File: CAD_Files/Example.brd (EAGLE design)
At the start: 86 x 54 mm, 14 parts, among them IC1 LM555D, J2 UX60-MB-5S8, Q1 BSS806N, Q2 SSM3J356R, SW1 MFS101D-6-Z

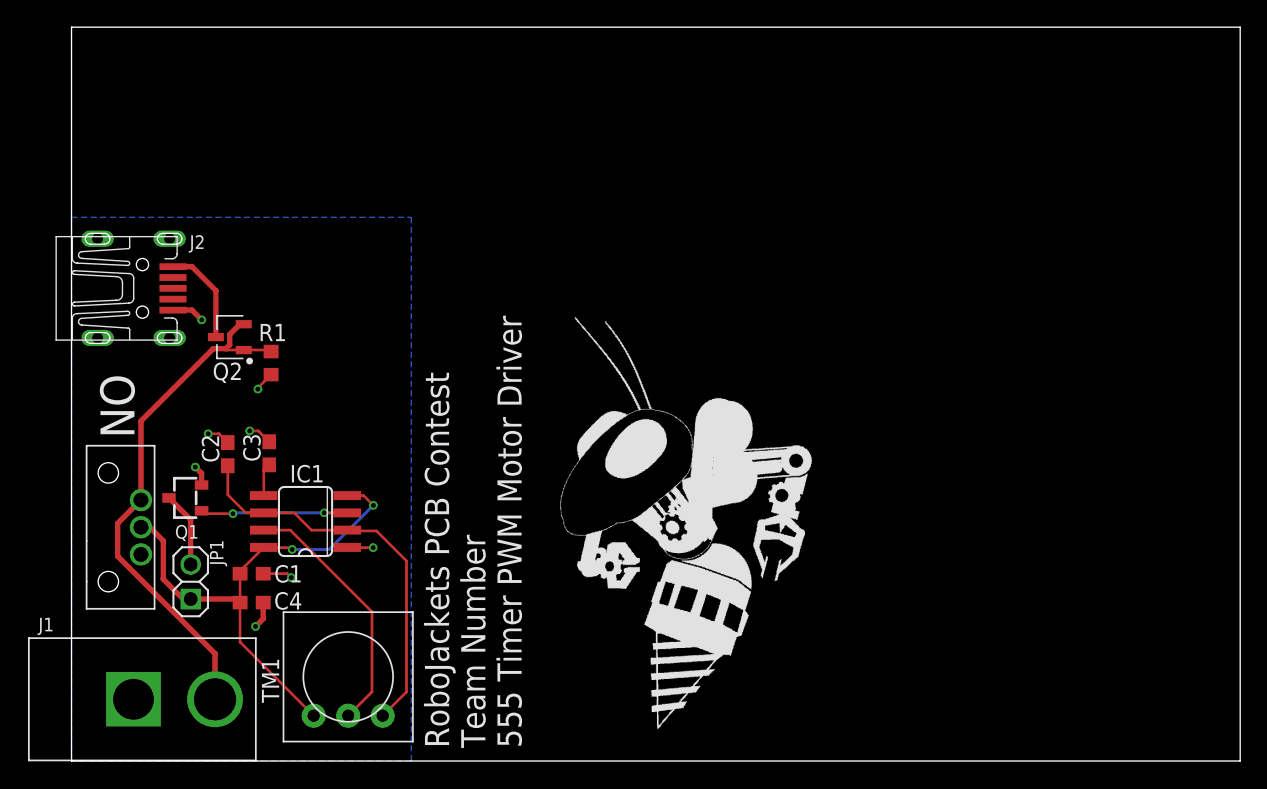
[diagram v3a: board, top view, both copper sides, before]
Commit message: Adjusted example to be final dimensions and fixed silkscreen
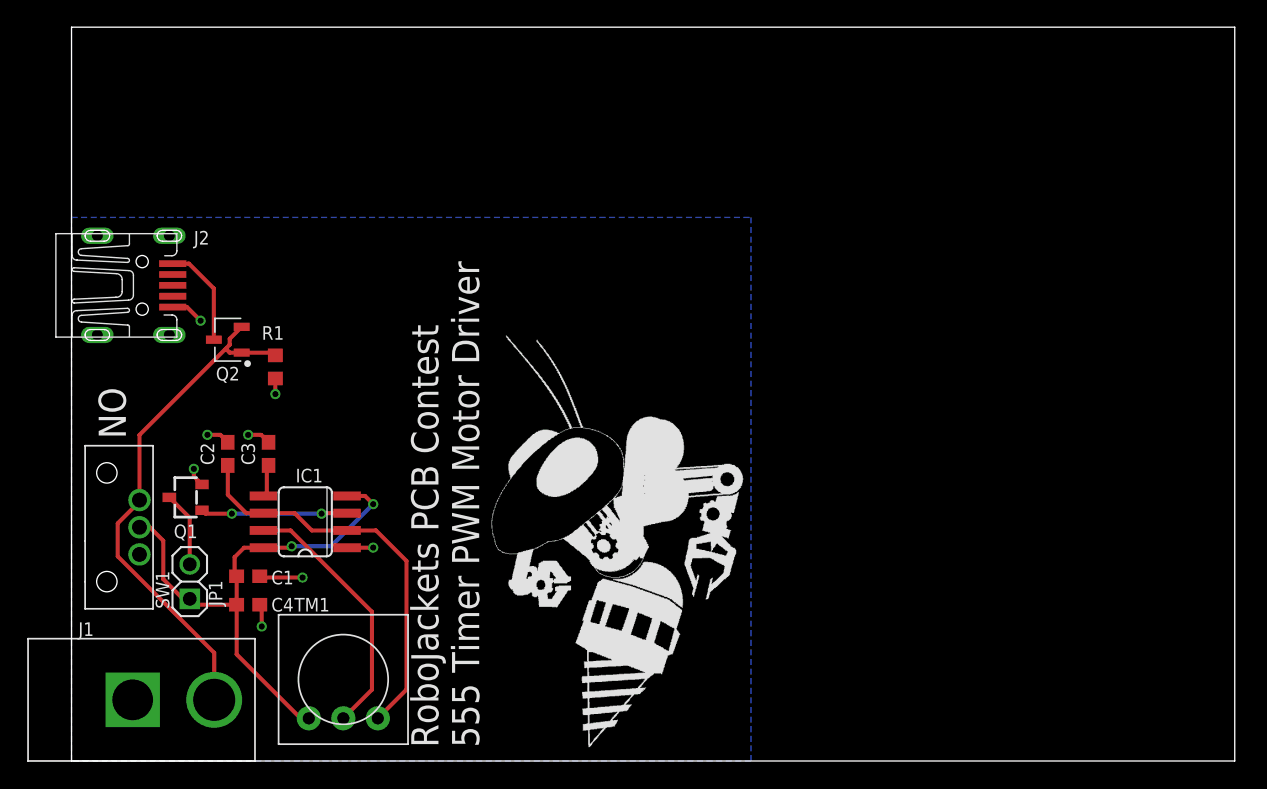
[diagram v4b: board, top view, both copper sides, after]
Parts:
- moved U$2 5.24 mm to (38.0, 1.00)
- moved R1 0.42 mm to (15.0, 29.0)
- moved TM1 0.41 mm to (20.0, 6.00)
- moved C1 0.31 mm to (13.0, 13.6)
- moved C4 0.30 mm to (13.0, 11.5)
- moved Q2 0.24 mm to (11.5, 31.0)
- moved J2 0.22 mm to (-1.20, 35.0)
- moved SW1 0.11 mm to (5.00, 17.2)
- moved J1 0.07 mm to (4.50, 4.50)
- moved JP1 0.07 mm to (8.70, 13.2)
- moved C3 0.06 mm to (14.5, 22.6)
- moved Q1 0.05 mm to (8.40, 19.4)
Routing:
- net +9V: track 38.3 -> 39.6 mm
- net N$6: track 38.5 -> 38.0 mm
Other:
- board size 86 x 54 mm -> 85.6 x 54 mm
- board text added: "RoboJackets PCB Contest 555 Timer PWM Motor Driver"
- board text removed: "RoboJackets PCB Contest Team Number 555 Timer PWM Motor Driver"
